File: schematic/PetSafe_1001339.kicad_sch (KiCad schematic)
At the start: 148 parts, among them J1 ICSP, J3 PIR BOARD, J5 MOTOR, J6 DNP, Q1 FMOS3401A?, Q11 MMBTA55?, Q2 BC847B?, Q3 MMBTA55?, Q4 MMBTA55?, Q5 MMBTA55?, Q6 MMBTA55?, Q7 BC857C?, Q8 SIL3724A?, Q9 NPN option / DNP, U1 S-1200B45?, U106 U6A / LDO option, U2 SN74LVC2G14DBV?, U3 SGM8542XS, U4 PIC16F18855, U5 MX512H, U6 S-812C33AMC? / 3.3V, U7 DNP, Y1 20 MHz

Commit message: Record Q8 supply continuity and stage S1 contact checks
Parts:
- C6: CurrentEvidence (none) -> C6 is photo-supported in parallel with C5 across H_RF_VDD/G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; Evidence Photo reconstruction; individual net evidence in reconstruc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 -> C6 is photo-supported in parallel with C5 across H_RF_VDD/G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
- Q8: CurrentEvidence 3724A supports the SIL3724A complementary MOSFET candidate; fitted maker unconfirmed. V113/V115 centre B2/native5 GND is resolved; outer-drain join retains D-E low-resistance evidence. V114 belongs to U2.T2 GND, not Q8. C6 is photo-supported in parallel with C5 as of v0.9.18. Q8 source-supply path remains independently qualified; no current centre-ground conflict. -> 3724A supports the SIL3724A complementary MOSFET candidate; fitted maker unconfirmed. B37 P-F = 1 ohm supports Q8.T2/native2 joining C6.1 on H_RF_VDD. The earlier 10-ohm reading is superseded for the current connection assessment; no fresh probe baseline or stability statement was supplied. V113/V115 centre B2/native5 GND and the outer-drain join retain earlier evidence; V114 belongs to U2.T2. Candidate pin functions, gate drive and operating levels remain unverified.; Evidence 3724A supports the SIL3724A complementary MOSFET candidate; fitted maker unconfirmed. V113/V115 centre B2/native5 GND is resolved; outer-drain join retains D-E low-resistance evidence. V114 belongs to U2.T2 GND, not Q8. C6 is photo-supported in parallel with C5 as of v0.9.18. Q8 source-supply path remains independently qualified; no current centre-ground conflict. -> 3724A supports the SIL3724A complementary MOSFET candidate; fitted maker unconfirmed. B37 P-F = 1 ohm supports Q8.T2/native2 joining C6.1 on H_RF_VDD. The earlier 10-ohm reading is superseded for the current connection assessment; no fresh probe baseline or stability statement was supplied. V113/V115 centre B2/native5 GND and the outer-drain join retain earlier evidence; V114 belongs to U2.T2. Candidate pin functions, gate drive and operating levels remain unverified.
- Q8: Evidence 3724A supports the SIL3724A complementary MOSFET candidate; fitted maker unconfirmed. V113/V115 centre B2/native5 GND is resolved; outer-drain join retains D-E low-resistance evidence. V114 belongs to U2.T2 GND, not Q8. C6 is photo-supported in parallel with C5 as of v0.9.18. Q8 source-supply path remains independently qualified; no current centre-ground conflict. -> 3724A supports the SIL3724A complementary MOSFET candidate; fitted maker unconfirmed. B37 P-F = 1 ohm supports Q8.T2/native2 joining C6.1 on H_RF_VDD. The earlier 10-ohm reading is superseded for the current connection assessment; no fresh probe baseline or stability statement was supplied. V113/V115 centre B2/native5 GND and the outer-drain join retain earlier evidence; V114 belongs to U2.T2. Candidate pin functions, gate drive and operating levels remain unverified.
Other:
- note added: "C6 parallels C5 (photo); Q8 P-F = 1 ohm supports H_RF_VDD join. Gate drive unverified."
- note added: "H07: C14R inverter candidate. C6 parallels C5 by photo; Q8 source rail supported by B37."
- note added: "v0.9.33 | KiCad 10.0.5 | 2026-10-09"
- note removed: "C6 parallels C5 on H_RF_VDD/GND (photo-supported). Q8 F-P 10 ohm path still qualified."
- note removed: "H07: C14R inverter candidate. C6 parallels C5 by photo; Q8 source rail still inferred."
- note removed: "v0.9.32 | KiCad 10.0.5 | 2026-10-09"

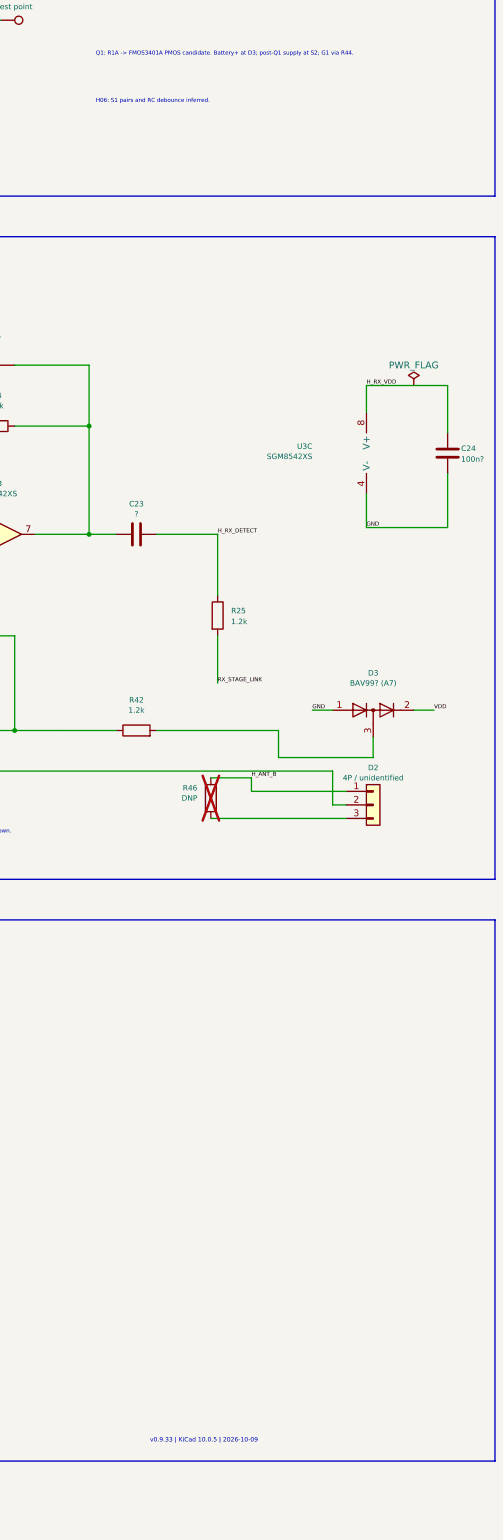
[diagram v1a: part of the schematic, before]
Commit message: Verify S1 contacts and close E05; prepare LED colour checks
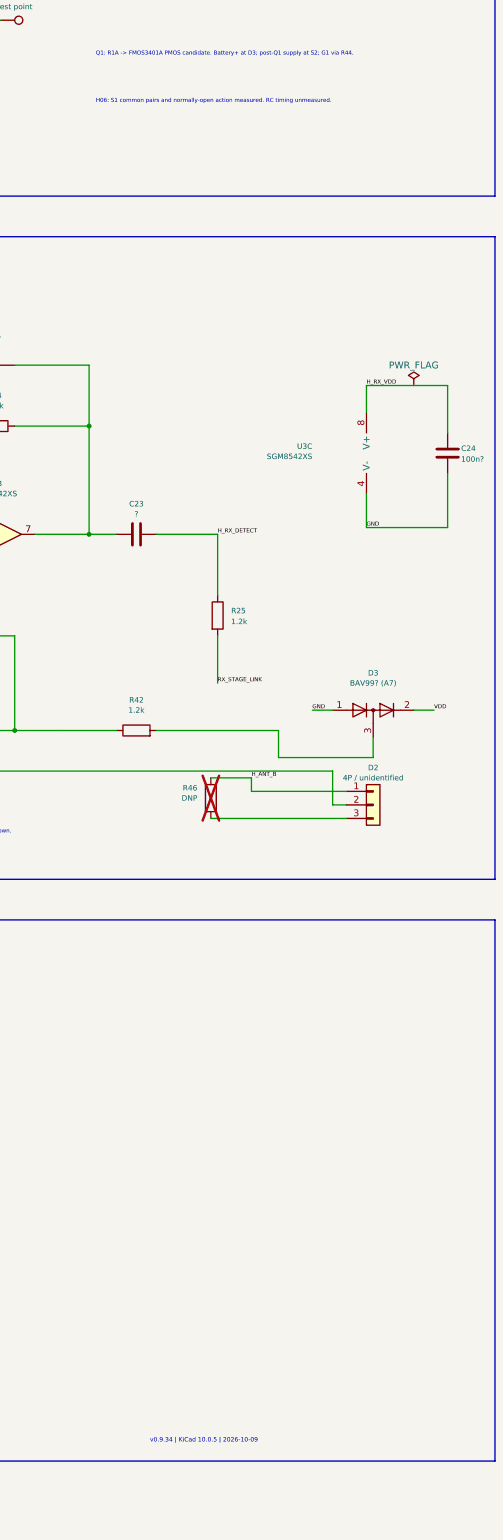
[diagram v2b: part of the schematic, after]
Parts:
- Q8: CurrentEvidence 3724A supports the SIL3724A complementary MOSFET candidate; fitted maker unconfirmed. V113/V115 centre B2/native5 GND is resolved; outer-drain join retains D-E low-resistance evidence. V114 belongs to U2.T2 GND, not Q8. C6 is photo-supported in parallel with C5 as of v0.9.18. Q8 source-supply path remains independently qualified; no current centre-ground conflict. -> 3724A supports the SIL3724A complementary MOSFET candidate; fitted maker unconfirmed. B37 P-F = 1 ohm supports Q8.T2/native2 joining C6.1 on H_RF_VDD. The earlier 10-ohm reading is superseded for the current connection assessment; no fresh probe baseline or stability statement was supplied. V113/V115 centre B2/native5 GND and the outer-drain join retain earlier evidence; V114 belongs to U2.T2. Candidate pin functions, gate drive and operating levels remain unverified.
- S1: ContactEvidence (none) -> B38 A-B 1 ohm; B39 C-D 1 ohm; B40 B-D released OL; B41 B-D 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; CurrentEvidence Measured body 6 x 6 x 4 mm plus 2 mm actuator. Stock SW_Pus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 -> B38-B41: A-B and C-D each 1 ohm; B-D released OL and held p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; Evidence Measured body 6 x 6 x 4 mm plus 2 mm actuator. Stock SW_Pus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 -> B38-B41: A-B and C-D each 1 ohm; B-D released OL and held p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
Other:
- note added: "H06: S1 common pairs and normally-open action measured. RC timing unmeasured."
- note added: "v0.9.34 | KiCad 10.0.5 | 2026-10-09"
- note removed: "H06: S1 pairs and RC debounce inferred."
- note removed: "v0.9.33 | KiCad 10.0.5 | 2026-10-09"

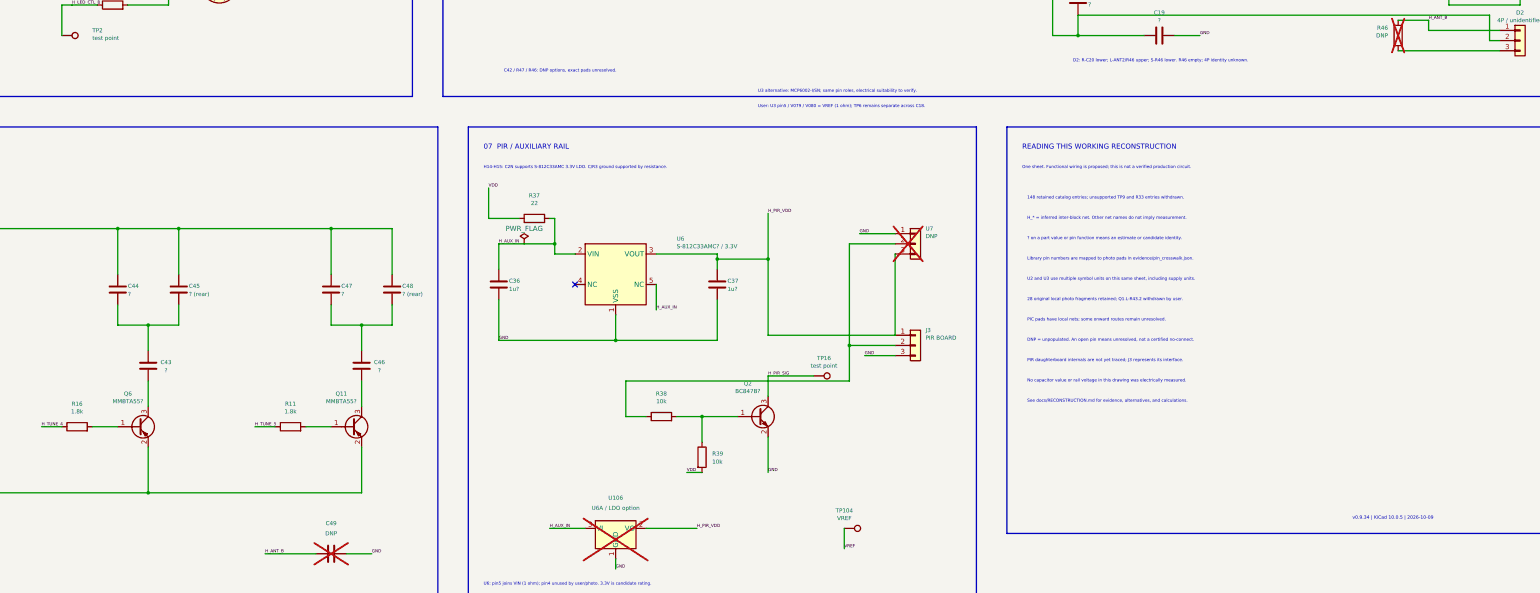
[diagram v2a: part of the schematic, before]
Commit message: Record LED1 red and green channel mapping; close colour checks
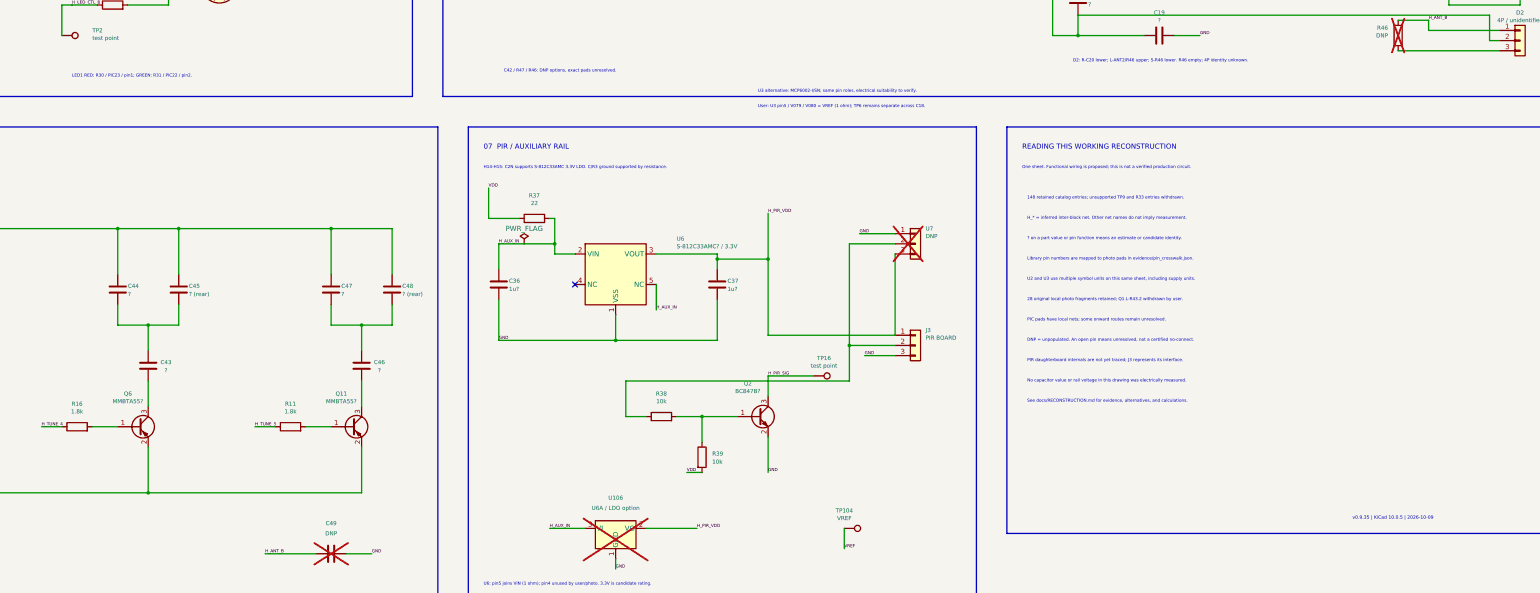
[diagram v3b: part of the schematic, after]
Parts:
- LED1: ColourEvidence (none) -> User B42/B43 colour observations, 2026-10-09; evidence/led1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; ColourMapping (none) -> Native pin1 / R30 / PIC23 = RED; native pin2 / R31 / PIC22 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; CurrentEvidence User confirms square 1.5 x 1.5 mm package containing red an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 -> B42/B43 user diode-mode colour report: photo A-K lights GRE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; Evidence User confirms square 1.5 x 1.5 mm package containing red an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 -> B42/B43 user diode-mode colour report: photo A-K lights GRE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
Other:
- note added: "LED1 RED: R30 / PIC23 / pin1; GREEN: R31 / PIC22 / pin2."
- note added: "v0.9.35 | KiCad 10.0.5 | 2026-10-09"
- note removed: "v0.9.34 | KiCad 10.0.5 | 2026-10-09"
